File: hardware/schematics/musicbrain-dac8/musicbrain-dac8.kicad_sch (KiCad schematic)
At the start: 26 parts, among them J1 BUS, J2 CV OUT, U1 AD5754BREZ, U2 AD5754BREZ, U3 ADR421

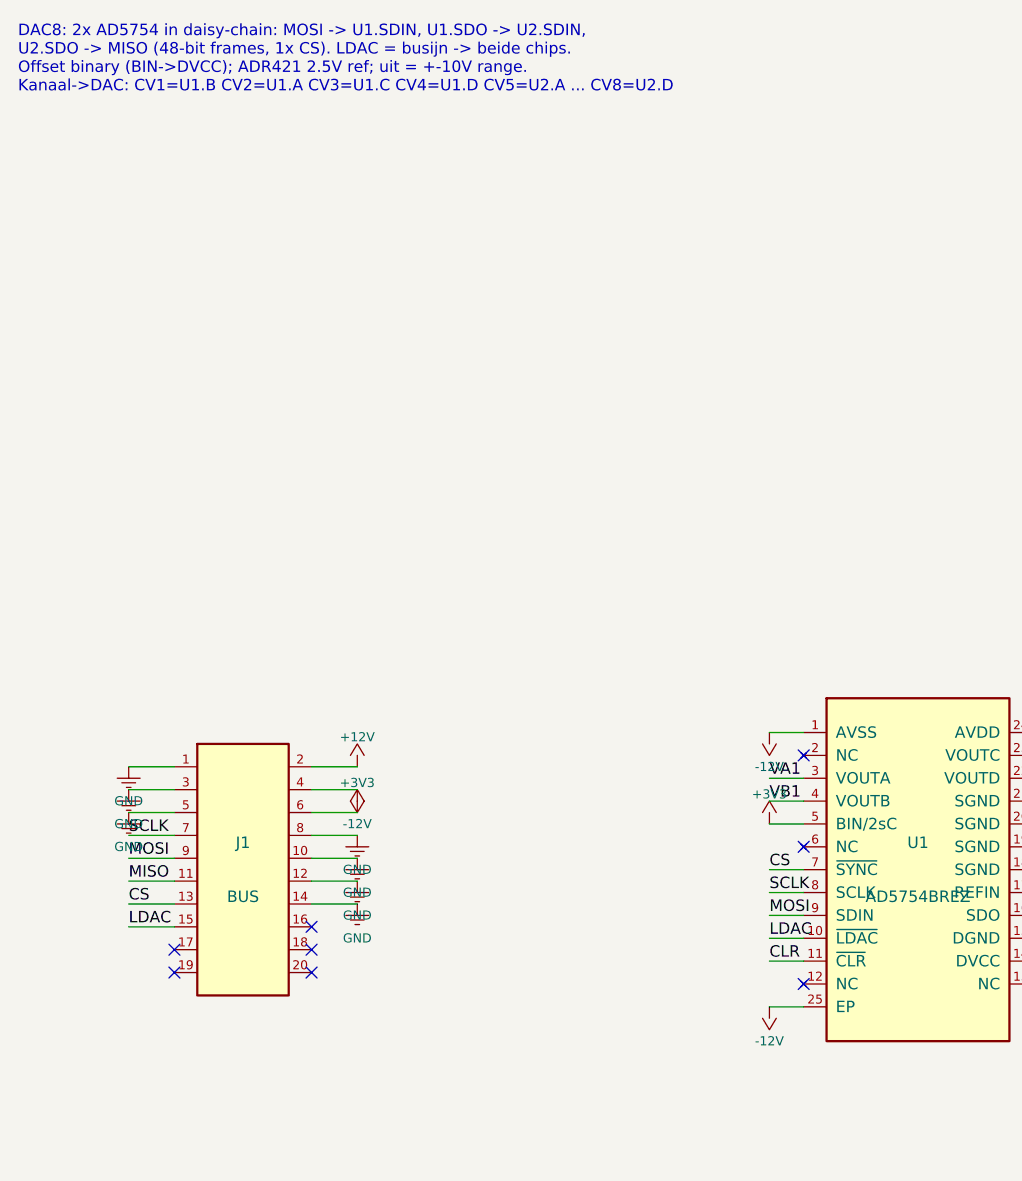
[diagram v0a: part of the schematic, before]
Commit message: dac8 gen 2: 80x45, slot 2x12, freerouting + DGND-redding
- kaart 50x80 -> 80x45; J1 2x10 -> 2x12 via bus.j1_map; J2 gecentreerd
- DACs onder hun CV-kolommen (U1 -> CV1-4, U2 -> CV5-8); handroutes
  vervangen door freerouting-SES
- DGND-redding (gen-1-les terug): pin 15 zit klem tussen de 0.65-entries;
  vast spoor + via voor freerouting uit
- C5/C13 GND-pad naar de open zuidcorridor (rot 270)
- prep_dsn: keepout-optie toegevoegd maar UIT - freerouting v2.1 meldt
  0 incompleet terwijl netten breken zodra er keepouts in de DSN staan
- ERC 0, netcheck OK, DRC 0/0

Co-Authored-By: Claude Fable 5 <noreply@anthropic.com>
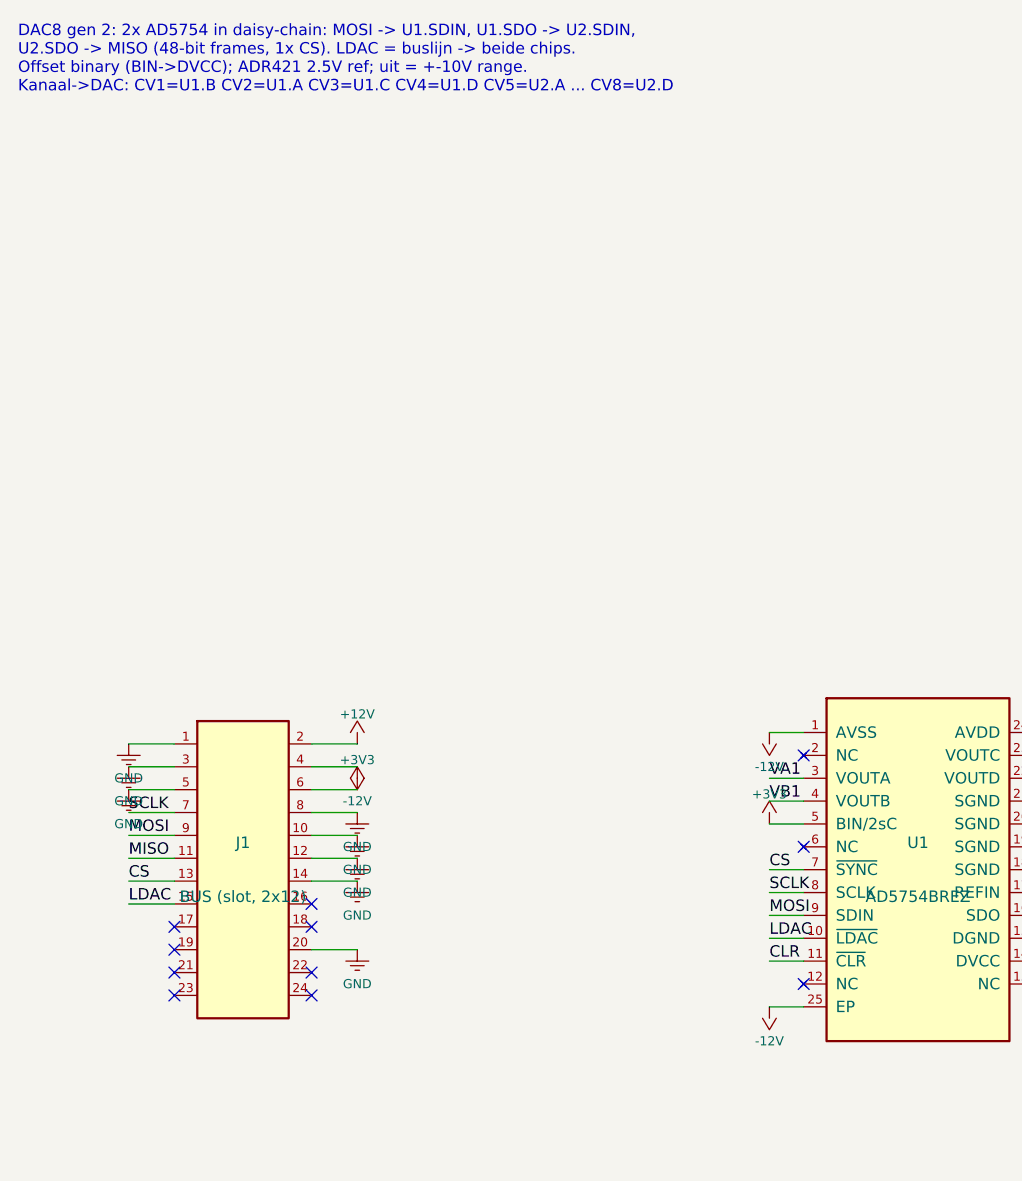
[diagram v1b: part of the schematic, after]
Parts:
- removed R1: 10k, Resistor_SMD:R_0805_2012Metric, symbol Device:R
- added C14: 10u, Capacitor_SMD:CP_Elec_4x5.3, symbol Device:C_Polarized
- C1: renamed from C2; value 100n -> 10u; footprint Capacitor_SMD:C_0805_2012Metric -> Capacitor_SMD:CP_Elec_4x5.3; symbol Device:C -> Device:C_Polarized
- C13: renamed from C14; value 10u -> 100n; footprint Capacitor_SMD:CP_Elec_4x5.3 -> Capacitor_SMD:C_0805_2012Metric; symbol Device:C_Polarized -> Device:C
- C2: renamed from C3; value 10u -> 100n; footprint Capacitor_SMD:CP_Elec_4x5.3 -> Capacitor_SMD:C_0805_2012Metric; symbol Device:C_Polarized -> Device:C
- C3: renamed from C4; value 100n -> 10u; footprint Capacitor_SMD:C_0805_2012Metric -> Capacitor_SMD:CP_Elec_4x5.3; symbol Device:C -> Device:C_Polarized
- C7: renamed from C8; value 10u -> 100n; footprint Capacitor_SMD:CP_Elec_4x5.3 -> Capacitor_SMD:C_0805_2012Metric; symbol Device:C_Polarized -> Device:C
- C8: renamed from C10; value 100n -> 10u; footprint Capacitor_SMD:C_0805_2012Metric -> Capacitor_SMD:CP_Elec_4x5.3; symbol Device:C -> Device:C_Polarized
- J1: value BUS -> BUS (slot, 2x12); footprint Connector_PinHeader_2.54mm:PinHeader_2x10_P2.54mm_Horizontal -> Connector_PinHeader_2.54mm:PinHeader_2x12_P2.54mm_Horizontal; symbol Custom:Conn_02x10 -> Custom:Conn_02x12
- R1: renamed from R2; value 100R -> 10k
- R9: renamed from C1; value 10u -> 100R; footprint Capacitor_SMD:CP_Elec_4x5.3 -> Resistor_SMD:R_0805_2012Metric; symbol Device:C_Polarized -> Device:R
- renumbered C12 to C10, C13 to C12, C5 to C4, C6 to C5, C7 to C6, R3 to R2, R4 to R3, R5 to R4, R6 to R5, R7 to R6, R8 to R7, R9 to R8
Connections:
- net +12V: now also C10.1, C2.1; no longer C6.1, R9.1 (+)
- net +3V3: now also C13.1, C5.1, R1.2; no longer C12.1, C4.1
- net -12V: now also C12.1, C4.1; no longer C10.1, C2.1 (+)
- net CLR: now also R1.1
- net CV1: now also R2.1; no longer R1.1
- net CV2: now also R3.1; no longer R2.1
- net CV3: now also R4.1; no longer R3.1
- net CV4: now also R5.1; no longer R4.1
- net CV5: now also R6.1; no longer R5.1
- net CV6: now also R7.1; no longer R6.1
- net CV7: now also R8.1; no longer R7.1
- net CV8: now also R9.1; no longer R8.1
- net GND: now also J1.20 (Pin_20), C14.2 (-); no longer R9.2 (-)
- net VA1: now also R3.2; no longer R2.2
- net VA2: now also R6.2; no longer R5.2
- net VB1: now also R2.2; no longer R1.2
- net VB2: now also R7.2; no longer R6.2
- net VC1: now also R4.2; no longer R3.2
- net VC2: now also R8.2; no longer R7.2
- net VD1: now also R5.2; no longer R4.2
- net VD2: now also R9.2; no longer R8.2
- net VREF: now also C6.1, C14.1 (+); no longer C13.1 (+), C5.1
- no-connect marks 13 -> 16
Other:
- note added: "DAC8 gen 2: 2x AD5754 in daisy-chain: MOSI -> U1.SDIN, U1.SDO -> U2.SDIN, U2.SDO -> MISO (48-bit frames, 1x CS). LDAC = buslijn -> beide chips. Offset binary (BIN->DVCC); ADR421 2.5V ref; uit = +-10V range. Kanaal->DAC: CV1=U1.B CV2=U1.A CV3=U1.C CV4=U1.D CV5=U2.A ... CV8=U2.D"
- note removed: "DAC8: 2x AD5754 in daisy-chain: MOSI -> U1.SDIN, U1.SDO -> U2.SDIN, U2.SDO -> MISO (48-bit frames, 1x CS). LDAC = busijn -> beide chips. Offset binary (BIN->DVCC); ADR421 2.5V ref; uit = +-10V range. Kanaal->DAC: CV1=U1.B CV2=U1.A CV3=U1.C CV4=U1.D CV5=U2.A ... CV8=U2.D"
- moved on the sheet: C10, C12, C4, C5, C6, R1, R2, R3, R4, R5, R6, R7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
